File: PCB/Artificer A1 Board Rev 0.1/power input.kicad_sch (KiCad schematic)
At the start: 71 parts, among them Q1 AON3419-TP, Q2 AON3419-TP, Q3 AO3401A, U1 GT-USB-7010ASV, U2 ESDA25W, U3 AP64500SP-13, U4 STUSB4500QTR, U5 AP64350SP-13, U6 AP64500SP-13, U7 10uH APH0630T100M

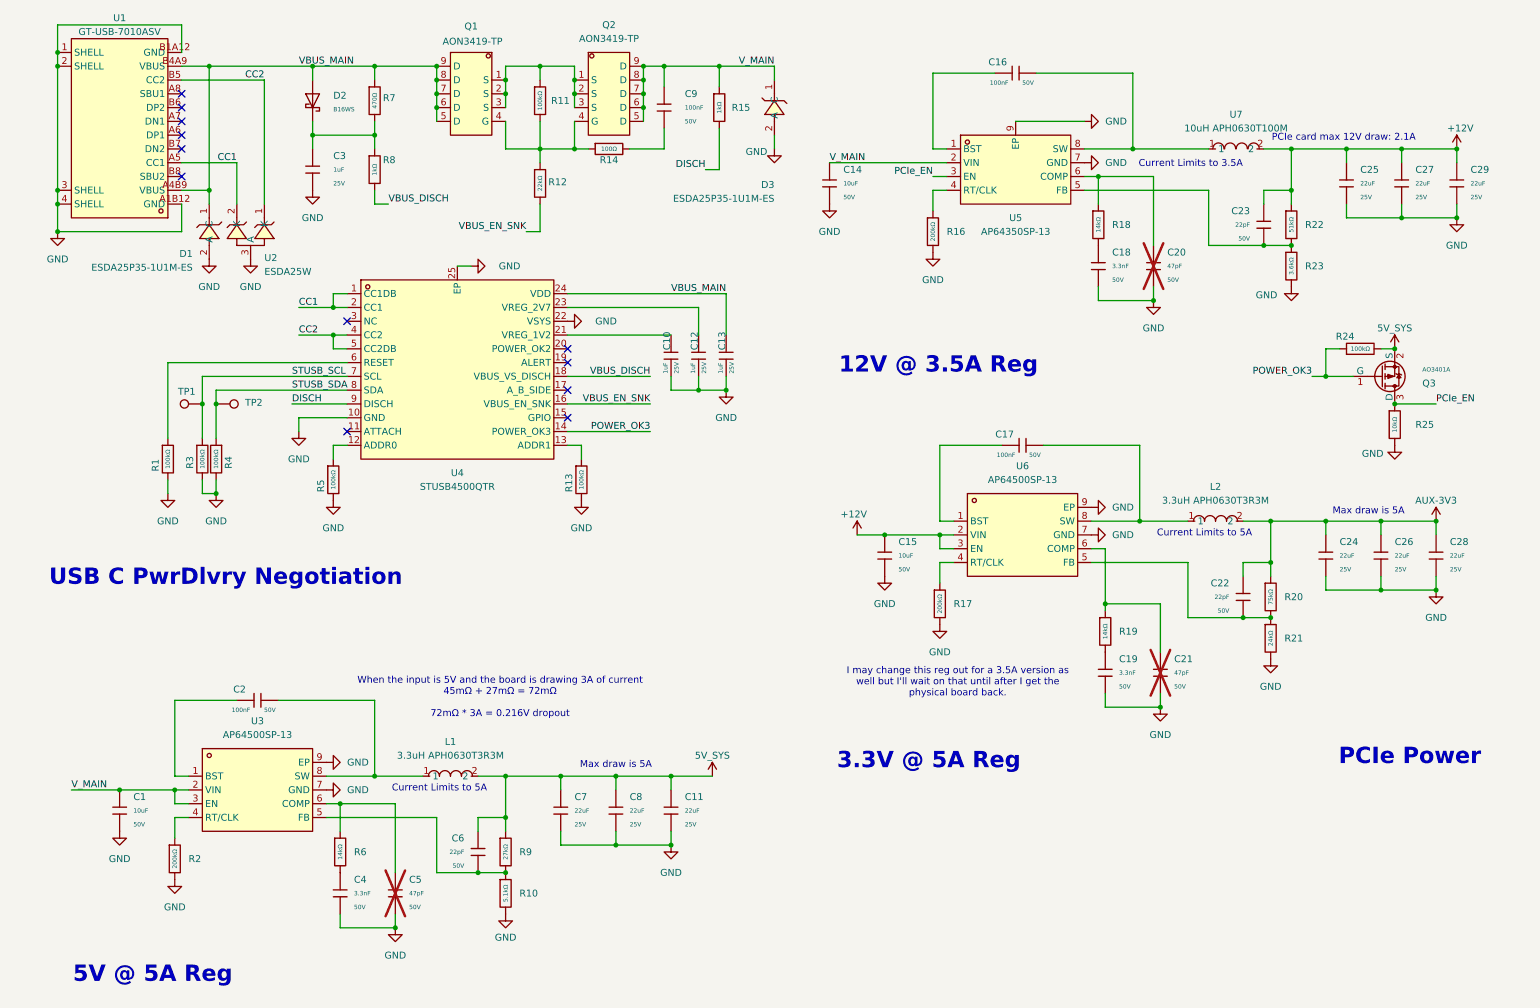
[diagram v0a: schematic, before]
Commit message: placed all components
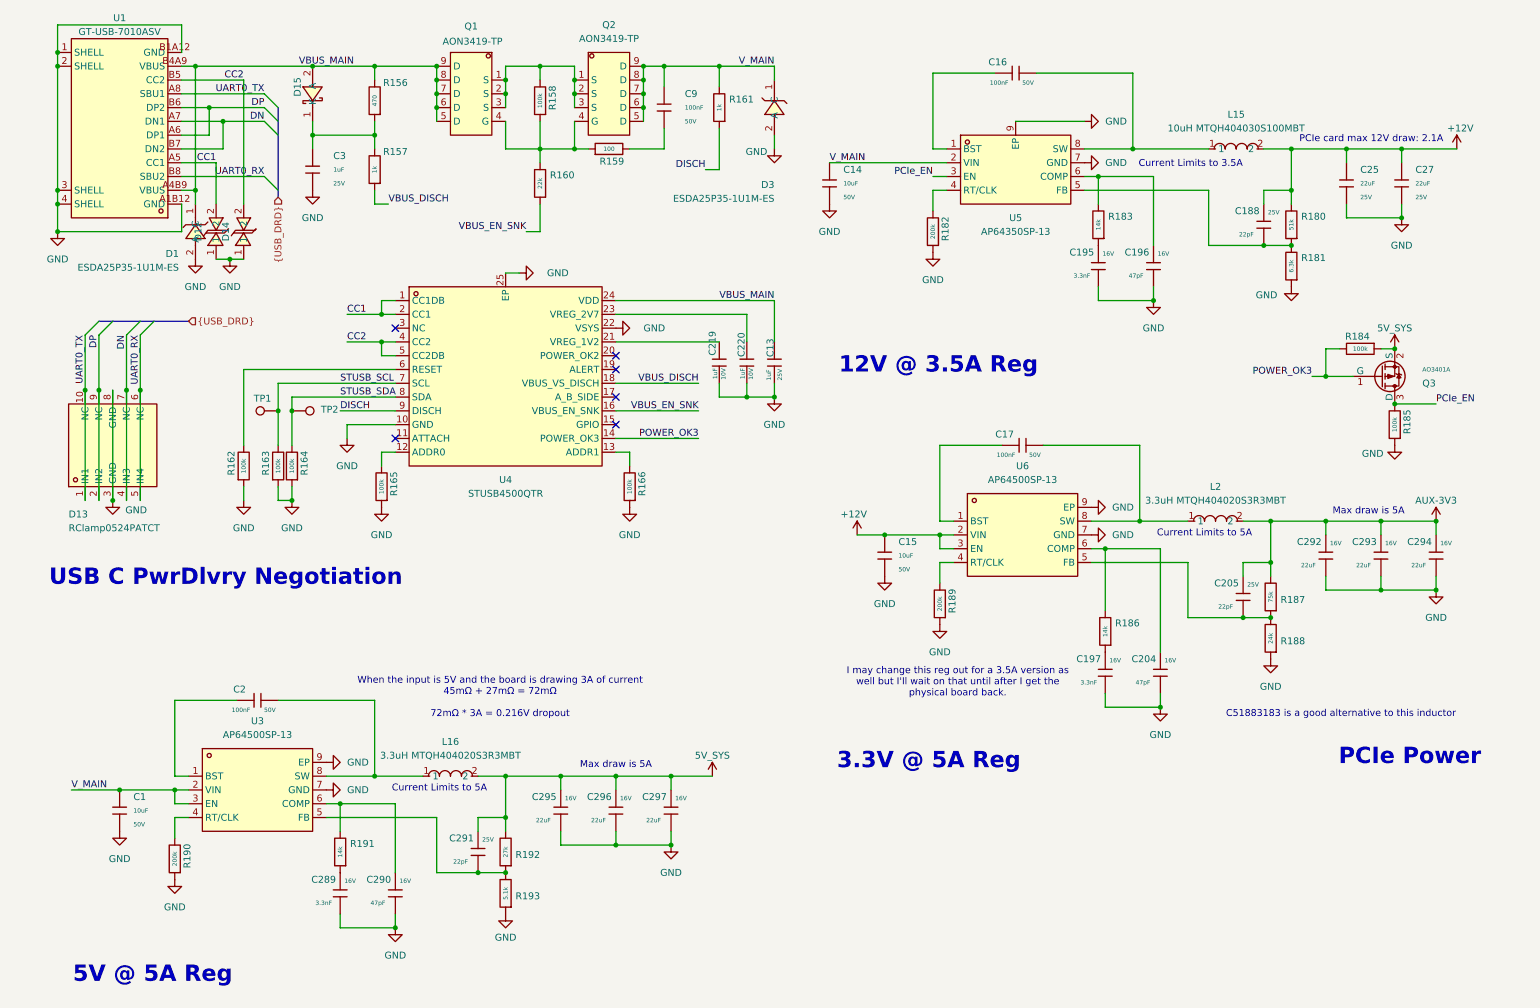
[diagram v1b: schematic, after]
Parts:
- removed C10, C12: 1uF, PCM_JLCPCB:C_0402, symbol PCM_JLCPCB-Capacitors:0402,1uF
- removed C11, C24, C26, C28, C29, C7, C8: 22uF, PCM_JLCPCB:C_0805, symbol PCM_JLCPCB-Capacitors:0805,22uF
- removed C18, C19, C4: 3.3nF, PCM_JLCPCB:C_0402, symbol PCM_JLCPCB-Capacitors:0402,3.3nF
- removed C20, C21, C5: 47pF, PCM_JLCPCB:C_0402, symbol PCM_JLCPCB-Capacitors:0402,47pF
- removed C22, C23, C6: 22pF, PCM_JLCPCB:C_0402, symbol PCM_JLCPCB-Capacitors:0402,22pF
- removed D2: B16WS, PCM_JLCPCB:D_SOD-323, symbol PCM_JLCPCB-Diodes:Schottky,B16WS
- removed L1, L2: 3.3uH APH0630T3R3M, easyeda:IND-SMD_L7.0-W6.6_APH0630, symbol easyeda:APH0630T3R3M
- removed R1, R11, R13, R24, R3, R4, R5: 100kΩ, PCM_JLCPCB:R_0402, symbol PCM_JLCPCB-Resistors:0402,100kΩ
- removed R10: 5.1kΩ, PCM_JLCPCB:R_0402, symbol PCM_JLCPCB-Resistors:0402,5.1kΩ
- removed R12: 22kΩ, PCM_JLCPCB:R_0402, symbol PCM_JLCPCB-Resistors:0402,22kΩ
- removed R14: 100Ω, PCM_JLCPCB:R_0402, symbol PCM_JLCPCB-Resistors:0402,100Ω
- removed R15, R8: 1kΩ, PCM_JLCPCB:R_0402, symbol PCM_JLCPCB-Resistors:0402,1kΩ
- removed R16, R17, R2: 200kΩ, PCM_JLCPCB:R_0402, symbol PCM_JLCPCB-Resistors:0402,200kΩ
- removed R18, R19, R6: 14kΩ, PCM_JLCPCB:R_0402, symbol PCM_JLCPCB-Resistors:0402,200kΩ
- removed R20: 75kΩ, PCM_JLCPCB:R_0402, symbol PCM_JLCPCB-Resistors:0402,75kΩ
- removed R21: 24kΩ, PCM_JLCPCB:R_0402, symbol PCM_JLCPCB-Resistors:0402,24kΩ
- removed R22: 51kΩ, PCM_JLCPCB:R_0402, symbol PCM_JLCPCB-Resistors:0402,51kΩ
- removed R23: 3.6kΩ, PCM_JLCPCB:R_0402, symbol PCM_JLCPCB-Resistors:0402,18kΩ
- removed R25: 10kΩ, PCM_JLCPCB:R_0402, symbol PCM_JLCPCB-Resistors:0402,10kΩ
- removed R7: 470Ω, PCM_JLCPCB:R_0402, symbol PCM_JLCPCB-Resistors:0402,470Ω
- removed R9: 27kΩ, PCM_JLCPCB:R_0402, symbol PCM_JLCPCB-Resistors:0402,27kΩ
- removed U2: ESDA25W, easyeda:SOT-323-3_L2.1-W1.3-P1.32-LS2.1-BR, symbol easyeda:ESDA25W
- removed U7: 10uH APH0630T100M, easyeda:IND-SMD_L7.1-W6.6, symbol easyeda:APH0630T100M
- added C188, C205, C291: 22pF, Capacitor_SMD:C_0201_0603Metric, symbol Cap:JLCPCB_Lib_Blank_Cap
- added C195, C197, C289: 3.3nF, Capacitor_SMD:C_0201_0603Metric, symbol Cap:JLCPCB_Lib_Blank_Cap
- added C196, C204, C290: 47pF, Capacitor_SMD:C_0201_0603Metric, symbol Cap:JLCPCB_Lib_Blank_Cap
- added C219, C220: 1uF, Capacitor_SMD:C_0201_0603Metric, symbol Cap:JLCPCB_Lib_Blank_Cap
- added C292, C293, C294, C295, C296, C297: 22uF, Capacitor_SMD:C_0603_1608Metric, symbol Cap:JLCPCB_Lib_Blank_Cap
- added D12, D14: LESD5D5.0CT1G_C5199850, easyeda:SOD-523_L1.2-W0.8-LS1.6-BI, symbol easyeda:LESD5D5.0CT1G_C5199850
- added D13: RClamp0524PATCT, easyeda:SLP2510P8_L2.5-W1.0-P0.50-BL, symbol easyeda:RClamp0524PATCT
- added D15: B5819WT_C7502714, easyeda:SOD-523_L1.2-W0.8-LS1.6-RD, symbol easyeda:B5819WT_C7502714
- added L15: 10uH MTQH404030S100MBT, easyeda:IND-SMD_L4.1-W4.1_MTQH404030S, symbol easyeda:MTQH404030S100MBT
- added L16, L2: 3.3uH MTQH404020S3R3MBT, easyeda:IND-SMD_L4.1-W4.1_MTQH404020S, symbol easyeda:MTQH404020S3R3MBT
- added R156: 470, Resistor_SMD:R_0201_0603Metric, symbol Cap:JLCPCB_Res_Custom
- added R157, R161: 1k, Resistor_SMD:R_0201_0603Metric, symbol Cap:JLCPCB_Res_Custom
- added R158, R162, R163, R164, R165, R166, R184, R185: 100k, Resistor_SMD:R_0201_0603Metric, symbol Cap:JLCPCB_Res_Custom
- added R159: 100, Resistor_SMD:R_0201_0603Metric, symbol Cap:JLCPCB_Res_Custom
- added R160: 22k, Resistor_SMD:R_0201_0603Metric, symbol Cap:JLCPCB_Res_Custom
- added R180: 51k, Resistor_SMD:R_0201_0603Metric, symbol Cap:JLCPCB_Res_Custom
- added R181: 6.3k, Resistor_SMD:R_0201_0603Metric, symbol Cap:JLCPCB_Res_Custom
- added R182, R189, R190: 200k, Resistor_SMD:R_0201_0603Metric, symbol Cap:JLCPCB_Res_Custom
- added R183, R186, R191: 14k, Resistor_SMD:R_0201_0603Metric, symbol Cap:JLCPCB_Res_Custom
- added R187: 75k, Resistor_SMD:R_0201_0603Metric, symbol Cap:JLCPCB_Res_Custom
- added R188: 24k, Resistor_SMD:R_0201_0603Metric, symbol Cap:JLCPCB_Res_Custom
- added R192: 27k, Resistor_SMD:R_0201_0603Metric, symbol Cap:JLCPCB_Res_Custom
- added R193: 5.1k, Resistor_SMD:R_0201_0603Metric, symbol Cap:JLCPCB_Res_Custom
- TP1, TP2: footprint TestPoint:TestPoint_Pad_D1.5mm -> TestPoint:TestPoint_Pad_D1.0mm
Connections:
- net +12V: now also C188.2, L15.2, R180.2
- net 5V_SYS: now also C291.2, C295.2, C296.2, C297.2, L16.2, R184.1, R192.2
- net AUX-3V3: now also C205.2, C292.2, C293.2, C294.2, L2.2, R187.2
- net CC1: now also D12.2
- net CC2: now also D14.2
- net DISCH: now also R161.1
- net GND: now also C195.1, C196.1, C197.1, C204.1, C219.1, C220.1, C289.1, C290.1, C292.1, C293.1, C294.1, C295.1, C296.1, C297.1, D12.1, D13.3 (GND), D13.8 (GND), D14.1, R162.1, R163.1, R164.1, R165.1, R166.1, R181.1, R182.1, R185.1, R188.1, R189.1, R190.1, R193.1
- net PCIe_EN: now also R185.2
- net POWER_OK3: now also R184.2
- net STUSB_SCL: now also R163.2
- net STUSB_SDA: now also R164.2
- net VBUS_DISCH: now also R157.1
- net VBUS_EN_SNK: now also R160.1
- net VBUS_MAIN: now also D15.2 (A), R156.2
- net V_MAIN: now also R161.2
- net at U5.4 (RT/CLK): now also R182.2
- net at U6.6 (COMP): now also C204.2, R186.2
- net at Q1.1 (S), Q1.2 (S), Q1.3 (S)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: now also R158.2
- net at Q1.4 (G), Q2.4 (G): now also R158.1, R159.1, R160.2
- net at U5.5 (FB): now also C188.1, R180.1, R181.2
- net at U5.6 (COMP): now also C196.2, R183.2
- net at C16.2, U5.8 (SW): now also L15.1
- net at C17.2, U6.8 (SW): now also L2.1
- net at U4.12 (ADDR0): now also R165.2
- net at U4.13 (ADDR1): now also R166.2
- net at U4.21 (VREG_1V2): now also C219.2
- net at U4.23 (VREG_2V7): now also C220.2
- net at U4.6 (RESET): now also R162.2
- net at U3.6 (COMP): now also C290.2, R191.2
- net at C2.2, U3.8 (SW): now also L16.1
- net at C3.1: now also D15.1 (K), R156.1, R157.2
- net at U3.5 (FB): now also C291.1, R192.1, R193.2
- net at U6.5 (FB): now also C205.1, R187.1, R188.2
- net at U6.4 (RT/CLK): now also R189.2
- net at U3.4 (RT/CLK): now also R190.2
- net at C9.2: now also R159.2
- net DP: now reaches U1.A6 (DP1)
- net DP: now also U1.B6 (DP2), D13.2 (IN2), D13.9 (NC)
- net DN: now reaches U1.A7 (DN1)
- net DN: now also U1.B7 (DN2), D13.4 (IN3), D13.7 (NC)
- net UART0_TX: now reaches U1.A8 (SBU1)
- net UART0_TX: now also D13.1 (IN1), D13.10 (NC)
- net UART0_RX: now reaches U1.B8 (SBU2)
- net UART0_RX: now also D13.5 (IN4), D13.6 (NC)
- new net: C289.2, R191.1
- new net: C197.2, R186.1
- new net: C195.2, R183.1
- no-connect marks 12 -> 6
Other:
- note added: "C51883183 is a good alternative to this inductor"
- moved on the sheet: C13, D1, TP1, TP2, U4

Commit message: finsihed more routing
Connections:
- net DN renamed DBG_DN
- net DP renamed DBG_DP
- net UART0_RX renamed DBG_UART0_RX
- net UART0_TX renamed DBG_UART0_TX
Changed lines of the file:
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@@
 		)
 	)
-	(label "UART0_TX"
+	(label "DBG_UART0_TX"
 		(at 21.59 73.66 270)
 		(effects
@@
 		)
 	)
-	(label "DP"
+	(label "DBG_DP"
 		(at 24.13 73.66 270)
 		(effects
@@
 		)
 	)
-	(label "UART0_RX"
+	(label "DBG_UART0_RX"
 		(at 31.75 73.66 270)
 		(effects
@@
 		)
 	)
-	(label "DN"
+	(label "DBG_DN"
 		(at 54.61 34.29 180)
 		(effects
@@
 		)
 	)
-	(label "DN"
+	(label "DBG_DN"
 		(at 29.21 73.66 270)
 		(effects
@@
 		)
 	)
-	(label "DP"
+	(label "DBG_DP"
 		(at 54.61 31.75 180)
 		(effects
@@
 		)
 	)
-	(label "UART0_TX"
+	(label "DBG_UART0_TX"
 		(at 54.61 29.21 180)
 		(effects
@@
 		)
 	)
-	(label "UART0_RX"
+	(label "DBG_UART0_RX"
 		(at 54.61 44.45 180)
 		(effects

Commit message: more power changed mipi csi and dis to aux 3.3V
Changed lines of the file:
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@@
 	(wire
 		(pts
-			(xy 193.04 34.29) (xy 205.74 34.29)
-		)
-		(stroke
-			(width 0)
-			(type default)
-		)
-	)
-	(wire
-		(pts
 			(xy 124.46 24.13) (xy 124.46 26.67)
 		)
@@
 	(wire
 		(pts
+			(xy 195.58 31.75) (xy 193.04 31.75)
+		)
+		(stroke
+			(width 0)
+			(type default)
+		)
+	)
+	(wire
+		(pts
 			(xy 219.71 113.03) (xy 209.55 113.03)
 		)
@@
 	(wire
 		(pts
+			(xy 193.04 31.75) (xy 193.04 34.29)
+		)
+		(stroke
+			(width 0)
+			(type default)
+		)
+	)
+	(wire
+		(pts
 			(xy 45.72 41.91) (xy 45.72 49.53)
 		)
@@
 	)
 	(symbol
-		(lib_id "easyeda:AP64350SP-13")
-		(at 193.04 41.91 0)
-		(unit 1)
-		(body_style 1)
-		(exclude_from_sim no)
-		(in_bom yes)
-		(on_board yes)
-		(in_pos_files yes)
-		(dnp no)
-		(fields_autoplaced yes)
-		(property "Reference" "U5"
-			(at 193.04 52.07 0)
-			(show_name no)
-			(do_not_autoplace no)
-			(effects
-				(font
-					(size 1.27 1.27)
-				)
-			)
-		)
-		(property "Value" "AP64350SP-13"
-			(at 193.04 54.61 0)
-			(show_name no)
-			(do_not_autoplace no)
-			(effects
-				(font
-					(size 1.27 1.27)
-				)
-			)
-		)
-		(property "Footprint" "easyeda:SO-8_L4.9-W3.9-P1.27-LS6.0-BL-EP"
-			(at 193.04 54.61 0)
-			(hide yes)
-			(show_name no)
-			(do_not_autoplace no)
-			(effects
-				(font
-					(size 1.27 1.27)
-				)
-			)
-		)
-		(property "Datasheet" "https://www.lcsc.com/datasheet/C2071691.pdf"
-			(at 193.04 57.15 0)
-			(hide yes)
-			(show_name no)
-			(do_not_autoplace no)
-			(effects
-				(font
-					(size 1.27 1.27)
-				)
-			)
-		)
-		(property "Description" ""
-			(at 193.04 41.91 0)
-			(hide yes)
-			(show_name no)
-			(do_not_autoplace no)
-			(effects
-				(font
-					(size 1.27 1.27)
-				)
-			)
-		)
-		(property "Manufacturer" "DIODES(美台)"
-			(at 193.04 59.69 0)
-			(hide yes)
-			(show_name no)
-			(do_not_autoplace no)
-			(effects
-				(font
-					(size 1.27 1.27)
-				)
-			)
-		)
-		(property "MPN" "AP64350SP-13"
-			(at 193.04 62.23 0)
-			(hide yes)
-			(show_name no)
-			(do_not_autoplace no)
-			(effects
-				(font
-					(size 1.27 1.27)
-				)
-			)
-		)
-		(property "LCSC Part" "C2071691"
-			(at 193.04 64.77 0)
-			(hide yes)
-			(show_name no)
-			(do_not_autoplace no)
-			(effects
-				(font
-					(size 1.27 1.27)
-				)
-			)
-		)
-		(pin "5"
-		)
-		(pin "9"
-		)
-		(pin "4"
-		)
-		(pin "8"
-		)
-		(pin "6"
-		)
-		(pin "7"
-		)
-		(pin "1"
-		)
-		(pin "3"
-		)
-		(pin "2"
-		)
-		(instances
-			(project "Artificer A1 Board Rev 0.1"
-				(path "/7c37bdb5-94b0-4567-b5ec-a879db855389/c4211ff5-fd83-42c8-a691-42056585a0db"
-					(reference "U5")
-					(unit 1)
-				)
-			)
-		)
-	)
-	(symbol
 		(lib_id "Cap:JLCPCB_Lib_Blank_Cap")
 		(at 138.43 78.74 180)
@@
 	(symbol
 		(lib_id "power:GND")
-		(at 205.74 34.29 90)
+		(at 195.58 31.75 90)
 		(unit 1)
 		(body_style 1)
@@
 		(fields_autoplaced yes)
 		(property "Reference" "#PWR027"
-			(at 212.09 34.29 0)
+			(at 201.93 31.75 0)
 			(hide yes)
 			(show_name no)
@@
 		)
 		(property "Value" "GND"
-			(at 209.55 34.2899 90)
+			(at 199.39 31.7499 90)
 			(show_name no)
 			(do_not_autoplace no)
@@
 		)
 		(property "Footprint" ""
-			(at 205.74 34.29 0)
+			(at 195.58 31.75 0)
 			(hide yes)
 			(show_name no)
@@
 		)
 		(property "Datasheet" ""
-			(at 205.74 34.29 0)
+			(at 195.58 31.75 0)
 			(hide yes)
 			(show_name no)
@@
 		)
 		(property "Description" "Power symbol creates a global label with name \"GND\" , ground"
-			(at 205.74 34.29 0)
+			(at 195.58 31.75 0)
 			(hide yes)
 			(show_name no)
@@
 					(unit 1)
 				)
+			)
+		)
+	)
+	(symbol
+		(lib_id "easyeda:AP64350SP-13")
+		(at 193.04 41.91 0)
+		(unit 1)
+		(body_style 1)
+		(exclude_from_sim no)
+		(in_bom yes)
+		(on_board yes)
+		(in_pos_files yes)
+		(dnp no)
+		(fields_autoplaced yes)
+		(property "Reference" "U5"
+			(at 193.04 52.07 0)
+			(show_name no)
+			(do_not_autoplace no)
+			(effects
+				(font
+					(size 1.27 1.27)
+				)
+			)
+		)
+		(property "Value" "AP64350SP-13"
+			(at 193.04 54.61 0)
+			(show_name no)
+			(do_not_autoplace no)
+			(effects
+				(font
+					(size 1.27 1.27)
+				)
+			)
+		)
+		(property "Footprint" "easyeda:SO-8_L4.9-W3.9-P1.27-LS6.0-BL-EP"
+			(at 193.04 54.61 0)
+			(hide yes)
+			(show_name no)
+			(do_not_autoplace no)
+			(effects
+				(font
+					(size 1.27 1.27)
+				)
+			)
+		)
+		(property "Datasheet" "https://www.lcsc.com/datasheet/C2071691.pdf"
+			(at 193.04 57.15 0)
+			(hide yes)
+			(show_name no)
+			(do_not_autoplace no)
+			(effects
+				(font
+					(size 1.27 1.27)
+				)
+			)
+		)
+		(property "Description" ""
+			(at 193.04 41.91 0)
+			(hide yes)
+			(show_name no)
+			(do_not_autoplace no)
+			(effects
+				(font
+					(size 1.27 1.27)
+				)
+			)
+		)
+		(property "Manufacturer" "DIODES(美台)"
+			(at 193.04 59.69 0)
+			(hide yes)
+			(show_name no)
+			(do_not_autoplace no)
+			(effects
+				(font
+					(size 1.27 1.27)
+				)
+			)
+		)
+		(property "MPN" "AP64350SP-13"
+			(at 193.04 62.23 0)
+			(hide yes)
+			(show_name no)
+			(do_not_autoplace no)
+			(effects
+				(font
+					(size 1.27 1.27)
+				)
+			)
+		)
+		(property "LCSC Part" "C2071691"
+			(at 193.04 64.77 0)
+			(hide yes)
+			(show_name no)
+			(do_not_autoplace no)
+			(effects
+				(font
+					(size 1.27 1.27)
+				)
+			)
+		)
+		(pin "3"
+		)
+		(pin "1"
+		)
+		(pin "6"
+		)
+		(pin "5"
+		)
+		(pin "4"
+		)
+		(pin "2"
+		)
+		(pin "9"
+		)
+		(pin "7"
+		)
+		(pin "8"
+		)
+		(instances
+			(project "Artificer A1 Board Rev 0.1"
+				(path "/7c37bdb5-94b0-4567-b5ec-a879db855389/c4211ff5-fd83-42c8-a691-42056585a0db"
+					(reference "U5")
+					(unit 1)
+				)

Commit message: added fan and PD debugging circuitry
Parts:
- removed TP1, TP2: TestPoint, TestPoint:TestPoint_Pad_D1.0mm, symbol Connector:TestPoint
- added CN2: B2B-PH-K-S, easyeda:CONN-TH_B2B-PH-K-S, symbol easyeda:B2B-PH-K-S
- added J3: Conn_02x02_Odd_Even, Connector_PinHeader_1.27mm:PinHeader_2x02_P1.27mm_Vertical, symbol Connector_Generic:Conn_02x02_Odd_Even
- added R241: 0Ω, Resistor_SMD:R_0201_0603Metric, symbol Cap:JLCPCB_Res_Custom
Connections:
- net 5V_SYS: now also CN2.1
- net GND: now also CN2.2, J3.2 (Pin_2), R241.1; no longer U4.22 (VSYS)
- net STUSB_SCL: now also J3.4 (Pin_4)
- net STUSB_SDA: now also J3.3 (Pin_3)
- new net VSYS: J3.1 (Pin_1), R241.2, U4.22 (VSYS)
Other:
- note added: "Fan 5V connector"

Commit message: optimized copper pour, added LEDs
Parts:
- added D16: GREEN LED, LED_SMD:LED_0402_1005Metric, symbol Device:LED
- added D2: RED LED, LED_SMD:LED_0402_1005Metric, symbol Device:LED
- added R242: 10k, Resistor_SMD:R_0201_0603Metric, symbol Cap:JLCPCB_Res_Custom
- added R243: 33k, Resistor_SMD:R_0201_0603Metric, symbol Cap:JLCPCB_Res_Custom
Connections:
- net +12V: now also R242.2
- net 5V_SYS: now also R243.2
- net GND: now also D16.1 (K), D2.1 (K)
- new net: D16.2 (A), R243.1
- new net: D2.2 (A), R242.1
